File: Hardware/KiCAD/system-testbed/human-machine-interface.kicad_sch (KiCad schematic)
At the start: 6 parts, among them IC1 PCF8575PWR, J1 Display Pin Socket, SW1 RotaryEncoder_Switch, X1 EYESPI, X2 EYESPI

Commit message: fix: reannotate schematics for pcb editor use #55
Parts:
- renumbered J1 to J3, X1 to X3, X2 to X4
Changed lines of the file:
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@@
 		(dnp no)
 		(fields_autoplaced yes)
-		(property "Reference" "#PWR012"
+		(property "Reference" "#PWR030"
 			(at 129.54 180.34 0)
 			(effects
@@
 			(project "system-testbed"
 				(path "/72756aea-0ff9-4757-9699-8d0f18588f6f/8dcdcb54-0a4a-4913-bd90-1e0f545b8046"
-					(reference "#PWR012")
+					(reference "#PWR030")
 					(unit 1)
 				)
@@
 		(dnp no)
 		(fields_autoplaced yes)
-		(property "Reference" "#PWR013"
+		(property "Reference" "#PWR031"
 			(at 143.51 31.75 0)
 			(effects
@@
 			(project "system-testbed"
 				(path "/72756aea-0ff9-4757-9699-8d0f18588f6f/8dcdcb54-0a4a-4913-bd90-1e0f545b8046"
-					(reference "#PWR013")
+					(reference "#PWR031")
 					(unit 1)
 				)
@@
 		(dnp no)
 		(fields_autoplaced yes)
-		(property "Reference" "#PWR010"
+		(property "Reference" "#PWR028"
 			(at 113.03 33.02 0)
 			(effects
@@
 			(project "system-testbed"
 				(path "/72756aea-0ff9-4757-9699-8d0f18588f6f/8dcdcb54-0a4a-4913-bd90-1e0f545b8046"
-					(reference "#PWR010")
+					(reference "#PWR028")
 					(unit 1)
 				)
@@
 		(on_board yes)
 		(dnp yes)
-		(property "Reference" "J1"
+		(property "Reference" "J3"
 			(at 54.61 40.005 0)
 			(effects
@@
 			(project "system-testbed"
 				(path "/72756aea-0ff9-4757-9699-8d0f18588f6f/8dcdcb54-0a4a-4913-bd90-1e0f545b8046"
-					(reference "J1")
+					(reference "J3")
 					(unit 1)
 				)
@@
 		(dnp no)
 		(fields_autoplaced yes)
-		(property "Reference" "#PWR026"
+		(property "Reference" "#PWR038"
 			(at 245.11 162.56 0)
 			(effects
@@
 			(project "system-testbed"
 				(path "/72756aea-0ff9-4757-9699-8d0f18588f6f/8dcdcb54-0a4a-4913-bd90-1e0f545b8046"
-					(reference "#PWR026")
+					(reference "#PWR038")
 					(unit 1)
 				)
@@
 		(dnp no)
 		(fields_autoplaced yes)
-		(property "Reference" "X1"
+		(property "Reference" "X3"
 			(at 90.17 48.895 90)
 			(effects
@@
 			(project "system-testbed"
 				(path "/72756aea-0ff9-4757-9699-8d0f18588f6f/8dcdcb54-0a4a-4913-bd90-1e0f545b8046"
-					(reference "X1")
+					(reference "X3")
 					(unit 1)
 				)
@@
 		(dnp no)
 		(fields_autoplaced yes)
-		(property "Reference" "#PWR01"
+		(property "Reference" "#PWR019"
 			(at 19.05 30.48 0)
 			(effects
@@
 			(project "system-testbed"
 				(path "/72756aea-0ff9-4757-9699-8d0f18588f6f/8dcdcb54-0a4a-4913-bd90-1e0f545b8046"
-					(reference "#PWR01")
+					(reference "#PWR019")
 					(unit 1)
 				)
@@
 		(dnp no)
 		(fields_autoplaced yes)
-		(property "Reference" "#PWR022"
+		(property "Reference" "#PWR034"
 			(at 222.25 162.56 0)
 			(effects
@@
 			(project "system-testbed"
 				(path "/72756aea-0ff9-4757-9699-8d0f18588f6f/8dcdcb54-0a4a-4913-bd90-1e0f545b8046"
-					(reference "#PWR022")
+					(reference "#PWR034")
 					(unit 1)
 				)
@@
 		(dnp no)
 		(fields_autoplaced yes)
-		(property "Reference" "X2"
+		(property "Reference" "X4"
 			(at 114.3 48.895 90)
 			(effects
@@
 			(project "system-testbed"
 				(path "/72756aea-0ff9-4757-9699-8d0f18588f6f/8dcdcb54-0a4a-4913-bd90-1e0f545b8046"
-					(reference "X2")
+					(reference "X4")
 					(unit 1)
 				)
@@
 		(dnp no)
 		(fields_autoplaced yes)
-		(property "Reference" "#PWR05"
+		(property "Reference" "#PWR023"
 			(at 62.23 179.07 0)
 			(effects
@@
 			(project "system-testbed"
 				(path "/72756aea-0ff9-4757-9699-8d0f18588f6f/8dcdcb54-0a4a-4913-bd90-1e0f545b8046"
-					(reference "#PWR05")
+					(reference "#PWR023")
 					(unit 1)
 				)
@@
 		(dnp no)
 		(fields_autoplaced yes)
-		(property "Reference" "#PWR02"
+		(property "Reference" "#PWR020"
 			(at 19.05 41.91 0)
 			(effects
@@
 			(project "system-testbed"
 				(path "/72756aea-0ff9-4757-9699-8d0f18588f6f/8dcdcb54-0a4a-4913-bd90-1e0f545b8046"
-					(reference "#PWR02")
+					(reference "#PWR020")
 					(unit 1)
 				)
@@
 		(dnp no)
 		(fields_autoplaced yes)
-		(property "Reference" "#PWR014"
+		(property "Reference" "#PWR032"
 			(at 143.51 43.18 0)
 			(effects
@@
 			(project "system-testbed"
 				(path "/72756aea-0ff9-4757-9699-8d0f18588f6f/8dcdcb54-0a4a-4913-bd90-1e0f545b8046"
-					(reference "#PWR014")
+					(reference "#PWR032")
 					(unit 1)
 				)
@@
 		(dnp no)
 		(fields_autoplaced yes)
-		(property "Reference" "#PWR07"
+		(property "Reference" "#PWR025"
 			(at 86.36 86.36 0)
 			(effects
@@
 			(project "system-testbed"
 				(path "/72756aea-0ff9-4757-9699-8d0f18588f6f/8dcdcb54-0a4a-4913-bd90-1e0f545b8046"
-					(reference "#PWR07")
+					(reference "#PWR025")
 					(unit 1)
 				)
@@
 		(dnp no)
 		(fields_autoplaced yes)
-		(property "Reference" "#PWR023"
+		(property "Reference" "#PWR035"
 			(at 227.33 162.56 0)
 			(effects
@@
 			(project "system-testbed"
 				(path "/72756aea-0ff9-4757-9699-8d0f18588f6f/8dcdcb54-0a4a-4913-bd90-1e0f545b8046"
-					(reference "#PWR023")
+					(reference "#PWR035")
 					(unit 1)
 				)
@@
 		(dnp no)
 		(fields_autoplaced yes)
-		(property "Reference" "#PWR06"
+		(property "Reference" "#PWR024"
 			(at 62.23 191.77 0)
 			(effects
@@
 			(project "system-testbed"
 				(path "/72756aea-0ff9-4757-9699-8d0f18588f6f/8dcdcb54-0a4a-4913-bd90-1e0f545b8046"
-					(reference "#PWR06")
+					(reference "#PWR024")
 					(unit 1)
 				)
@@
 		(dnp no)
 		(fields_autoplaced yes)
-		(property "Reference" "#PWR09"
+		(property "Reference" "#PWR027"
 			(at 106.68 179.07 0)
 			(effects
@@
 			(project "system-testbed"
 				(path "/72756aea-0ff9-4757-9699-8d0f18588f6f/8dcdcb54-0a4a-4913-bd90-1e0f545b8046"
-					(reference "#PWR09")
+					(reference "#PWR027")
 					(unit 1)
 				)
@@
 		(dnp no)
 		(fields_autoplaced yes)
-		(property "Reference" "#PWR024"
+		(property "Reference" "#PWR036"
 			(at 232.41 162.56 0)
 			(effects
@@
 			(project "system-testbed"
 				(path "/72756aea-0ff9-4757-9699-8d0f18588f6f/8dcdcb54-0a4a-4913-bd90-1e0f545b8046"
-					(reference "#PWR024")
+					(reference "#PWR036")
 					(unit 1)
 				)
@@
 		(dnp no)
 		(fields_autoplaced yes)
-		(property "Reference" "#PWR017"
+		(property "Reference" "#PWR033"
 			(at 161.29 193.04 0)
 			(effects
@@
 			(project "system-testbed"
 				(path "/72756aea-0ff9-4757-9699-8d0f18588f6f/8dcdcb54-0a4a-4913-bd90-1e0f545b8046"
-					(reference "#PWR017")
+					(reference "#PWR033")
 					(unit 1)
 				)
@@
 		(dnp no)
 		(fields_autoplaced yes)
-		(property "Reference" "#PWR03"
+		(property "Reference" "#PWR021"
 			(at 60.96 30.48 0)
 			(effects
@@
 			(project "system-testbed"
 				(path "/72756aea-0ff9-4757-9699-8d0f18588f6f/8dcdcb54-0a4a-4913-bd90-1e0f545b8046"
-					(reference "#PWR03")
+					(reference "#PWR021")
 					(unit 1)
 				)
@@
 		(on_board yes)
 		(dnp no)
-		(property "Reference" "#PWR025"
+		(property "Reference" "#PWR037"
 			(at 245.11 104.14 0)
 			(effects
@@
 			(project "system-testbed"
 				(path "/72756aea-0ff9-4757-9699-8d0f18588f6f/8dcdcb54-0a4a-4913-bd90-1e0f545b8046"
-					(reference "#PWR025")
+					(reference "#PWR037")
 					(unit 1)
 				)
@@
 		(dnp no)
 		(fields_autoplaced yes)
-		(property "Reference" "#PWR08"
+		(property "Reference" "#PWR026"
 			(at 93.98 33.02 0)
 			(effects
@@
 			(project "system-testbed"
 				(path "/72756aea-0ff9-4757-9699-8d0f18588f6f/8dcdcb54-0a4a-4913-bd90-1e0f545b8046"
-					(reference "#PWR08")
+					(reference "#PWR026")
 					(unit 1)
 				)
@@
 		(dnp no)
 		(fields_autoplaced yes)
-		(property "Reference" "#PWR04"
+		(property "Reference" "#PWR022"
 			(at 60.96 43.18 0)
 			(effects
@@
 			(project "system-testbed"
 				(path "/72756aea-0ff9-4757-9699-8d0f18588f6f/8dcdcb54-0a4a-4913-bd90-1e0f545b8046"
-					(reference "#PWR04")
+					(reference "#PWR022")
 					(unit 1)
 				)
@@
 		(dnp no)
 		(fields_autoplaced yes)
-		(property "Reference" "#PWR011"
+		(property "Reference" "#PWR029"
 			(at 118.11 86.36 0)
 			(effects
@@
 			(project "system-testbed"
 				(path "/72756aea-0ff9-4757-9699-8d0f18588f6f/8dcdcb54-0a4a-4913-bd90-1e0f545b8046"
-					(reference "#PWR011")
-					(unit 1)
-				)
+					(reference "#PWR029")
+					(unit 1)
+				)

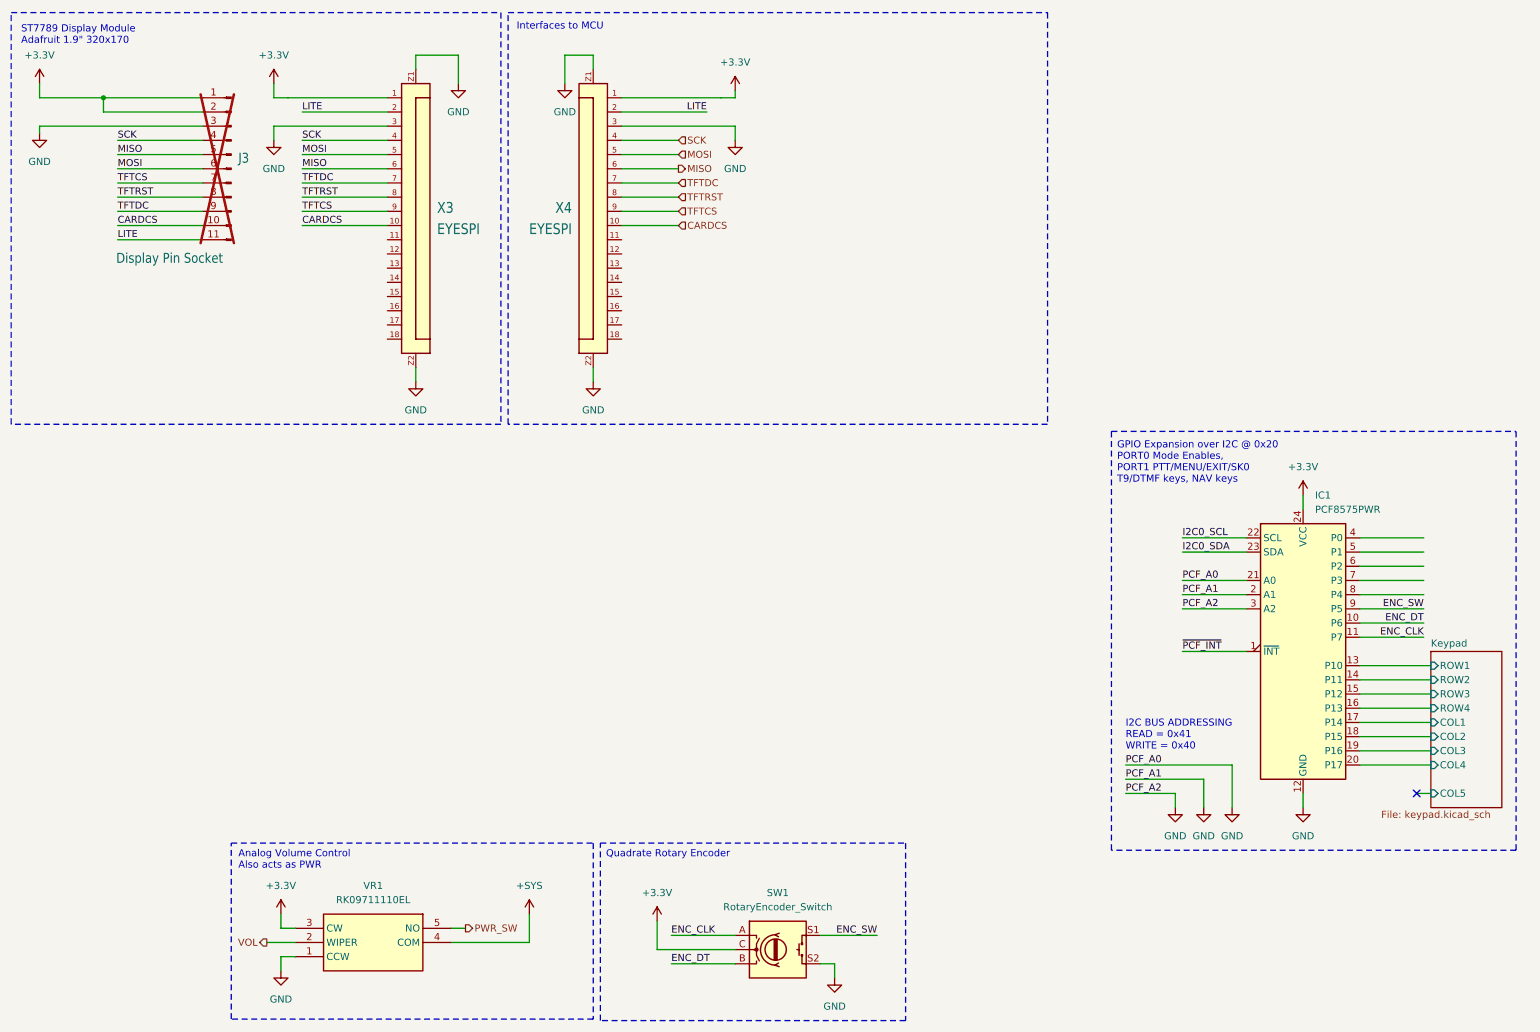
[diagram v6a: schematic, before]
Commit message: feat: swap to vertical rotary encoder used by Modulino Knob #69
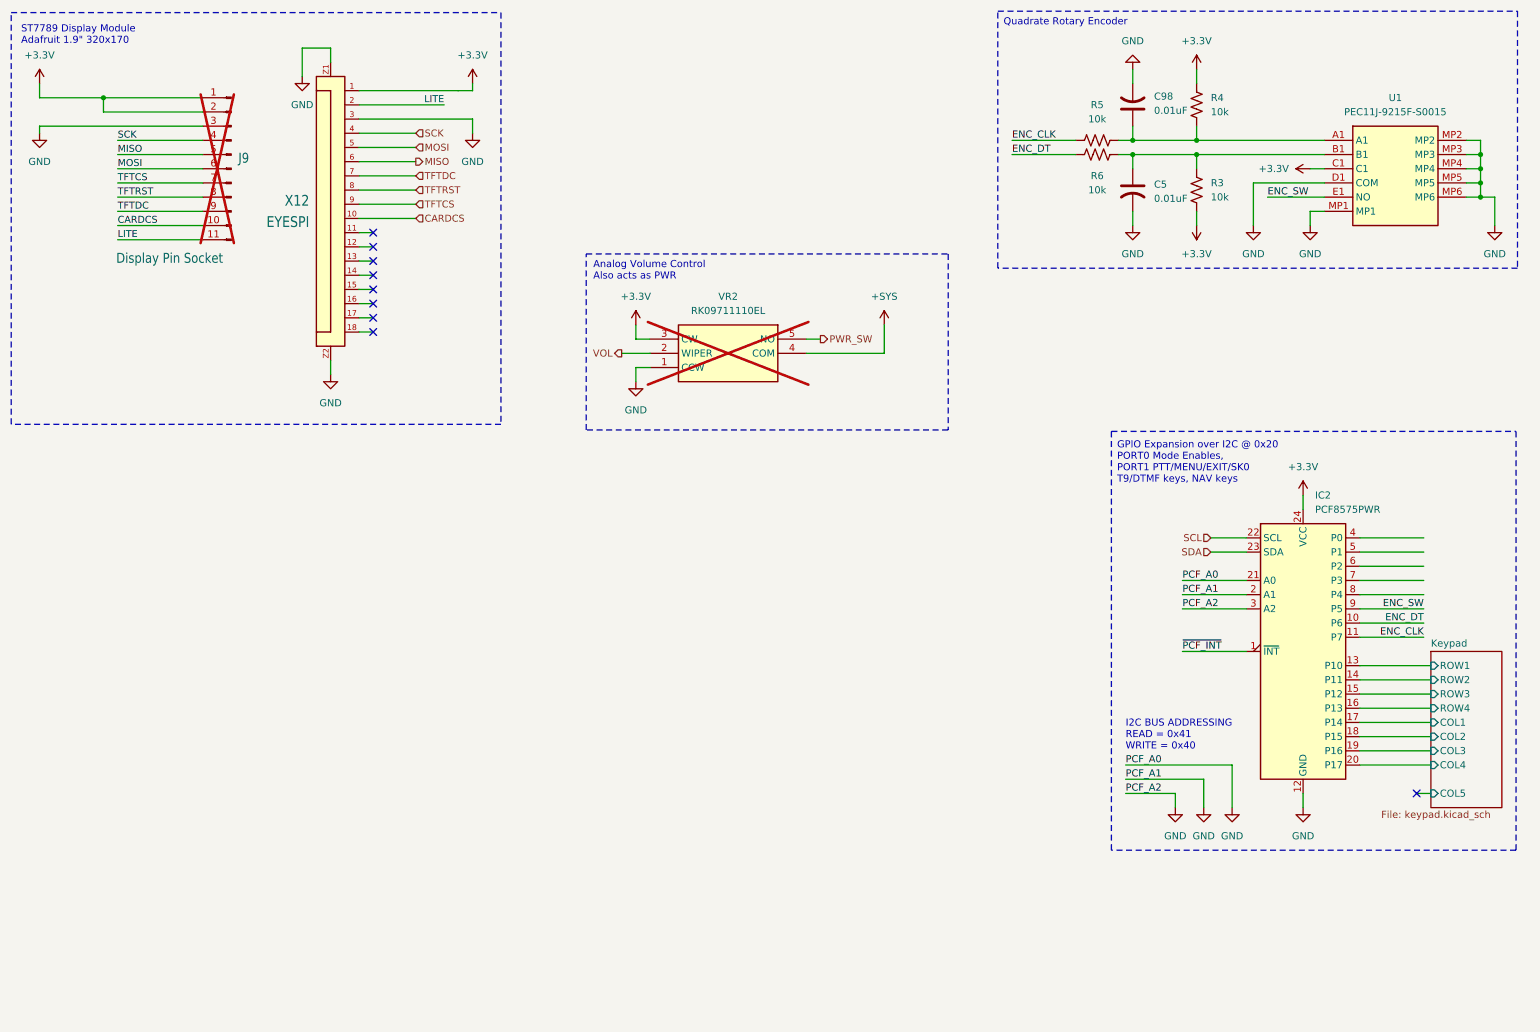
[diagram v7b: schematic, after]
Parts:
- removed SW1: RotaryEncoder_Switch, Rotary_Encoder:RotaryEncoder_Bourns_Horizontal_PEC12R-2x17F-Sxxxx, symbol Device:RotaryEncoder_Switch
- removed X3: EYESPI, capstone-project:Adafruit EYESPI FPC Connector, symbol capstone-project:Adafruit EYESPI FPC Connector
- added C5, C98: 0.01uF, Capacitor_SMD:C_0603_1608Metric, symbol Device:C_US
- added R3, R4, R5, R6: 10k, Resistor_SMD:R_0603_1608Metric, symbol Device:R_US
- added U1: PEC11J-9215F-S0015, capstone-project:PEC11J9215FS0015, symbol capstone-project:PEC11J-9215F-S0015
- J9: renamed from J3; footprint Display:1X11_ROUND_76 -> Connector_PinHeader_2.54mm:PinHeader_1x11_P2.54mm_Vertical
- VR2: renamed from VR1; now not fitted
- renumbered IC1 to IC2, X4 to X12
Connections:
- net +3.3V: now also R3.2, R4.1, U1.C1
- net ENC_CLK: now also R5.1
- net ENC_DT: now also R6.1
- net ENC_SW: now also U1.E1 (NO)
- net GND: now also C5.2, C98.2, U1.D1 (COM), U1.MP1, U1.MP2, U1.MP3, U1.MP4, U1.MP5, U1.MP6
- net I2C0_SCL renamed SCL
- net I2C0_SDA renamed SDA
- new net: C5.1, R3.1, R6.2, U1.B1
- new net: C98.1, R4.2, R5.2, U1.A1
- no-connect marks 1 -> 9
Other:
- note removed: "Interfaces to MCU"
- moved on the sheet: X12

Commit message: fix: allow for DRC use in PCB editor by successful reannotation
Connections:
- net TFTDC: now also IC2.5 (P1)
- net TFTRST: now also IC2.6 (P2)
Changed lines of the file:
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@@
 	(wire
 		(pts
-			(xy 86.36 43.18) (xy 76.2 43.18)
+			(xy 91.44 43.18) (xy 76.2 43.18)
 		)
 		(stroke
@@
 	(wire
 		(pts
-			(xy 86.36 45.72) (xy 76.2 45.72)
+			(xy 91.44 45.72) (xy 76.2 45.72)
 		)
 		(stroke
@@
 			(width 0)
 			(type default)
+		)
+	)
+	(label "TFTDC"
+		(at 266.7 110.49 180)
+		(effects
+			(font
+				(size 1.2446 1.2446)
+			)
+			(justify right bottom)
+		)
+	)
+	(label "TFTDC"
+		(at 91.44 43.18 180)
+		(effects
+			(font
+				(size 1.2446 1.2446)
+			)
+			(justify right bottom)
 		)
 	)
@@
 		)
 	)
+	(label "TFTRST"
+		(at 91.44 45.72 180)
+		(effects
+			(font
+				(size 1.2446 1.2446)
+			)
+			(justify right bottom)
+		)
+	)
 	(label "LITE"
 		(at 33.02 54.61 0)
@@
 			)
 			(justify left bottom)
+		)
+	)
+	(label "TFTRST"
+		(at 266.7 113.03 180)
+		(effects
+			(font
+				(size 1.2446 1.2446)
+			)
+			(justify right bottom)
 		)
 	)
@@
 		)
 	)
+	(hierarchical_label "SDA"
+		(shape input)
+		(at 228.6 110.49 180)
+		(effects
+			(font
+				(size 1.27 1.27)
+			)
+			(justify right)
+		)
+	)
+	(hierarchical_label "PWR_SW"
+		(shape output)
+		(at 158.75 72.39 0)
+		(effects
+			(font
+				(size 1.27 1.27)
+			)
+			(justify left)
+		)
+	)
 	(hierarchical_label "TFTCS"
 		(shape input)
@@
 		)
 	)
-	(hierarchical_label "SDA"
-		(shape input)
-		(at 228.6 110.49 180)
-		(effects
-			(font
-				(size 1.27 1.27)
-			)
-			(justify right)
-		)
-	)
 	(hierarchical_label "CARDCS"
 		(shape input)
@@
 		)
 	)
-	(hierarchical_label "PWR_SW"
-		(shape output)
-		(at 158.75 72.39 0)
-		(effects
-			(font
-				(size 1.27 1.27)
-			)
-			(justify left)
-		)
-	)
 	(hierarchical_label "SCL"
 		(shape input)
@@
 		)
 	)
-	(hierarchical_label "TFTRST"
-		(shape input)
-		(at 86.36 45.72 0)
-		(effects
-			(font
-				(size 1.2446 1.2446)
-			)
-			(justify left)
-		)
-	)
 	(hierarchical_label "SCK"
 		(shape input)
@@
 		(effects
 			(font
-				(size 1.2446 1.2446)
-			)
-			(justify left)
-		)
-	)
-	(hierarchical_label "TFTDC"
-		(shape input)
-		(at 86.36 43.18 0)
-		(effects
-			(font
